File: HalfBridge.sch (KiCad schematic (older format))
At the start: 5 parts, among them Q2 Q_NMOS_DGS, Q3 Q_NMOS_DGS, Q4 STS8DN6LF6AG

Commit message: Started work on layout
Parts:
- removed Q2, Q3: Q_NMOS_DGS, symbol Device:Q_NMOS_DGS
- added D70, D71: LED_Green, LED_SMD:LED_0805_2012Metric_Pad1.15x1.40mm_HandSolder, symbol Custom-Symbols:LED_Green
- added Q20, Q21: DMN62D0U-7, Package_TO_SOT_SMD:SOT-23, symbol Custom-Symbols:DMN62D0U-7
- added R41, R42: R, Resistor_SMD:R_0805_2012Metric, symbol Device:R
- R3, R4: footprint (none) -> Resistor_SMD:R_0805_2012Metric
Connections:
- net labels added: +5V, Gate_H, Gate_L
- net labels removed: Power, VCC
- wire segments 23 -> 27
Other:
- note added: "Drive Status LEDs"
- note added: "Power MOSFET Datasheet:"
- moved on the sheet: Q22A, Q22B, R15, R16

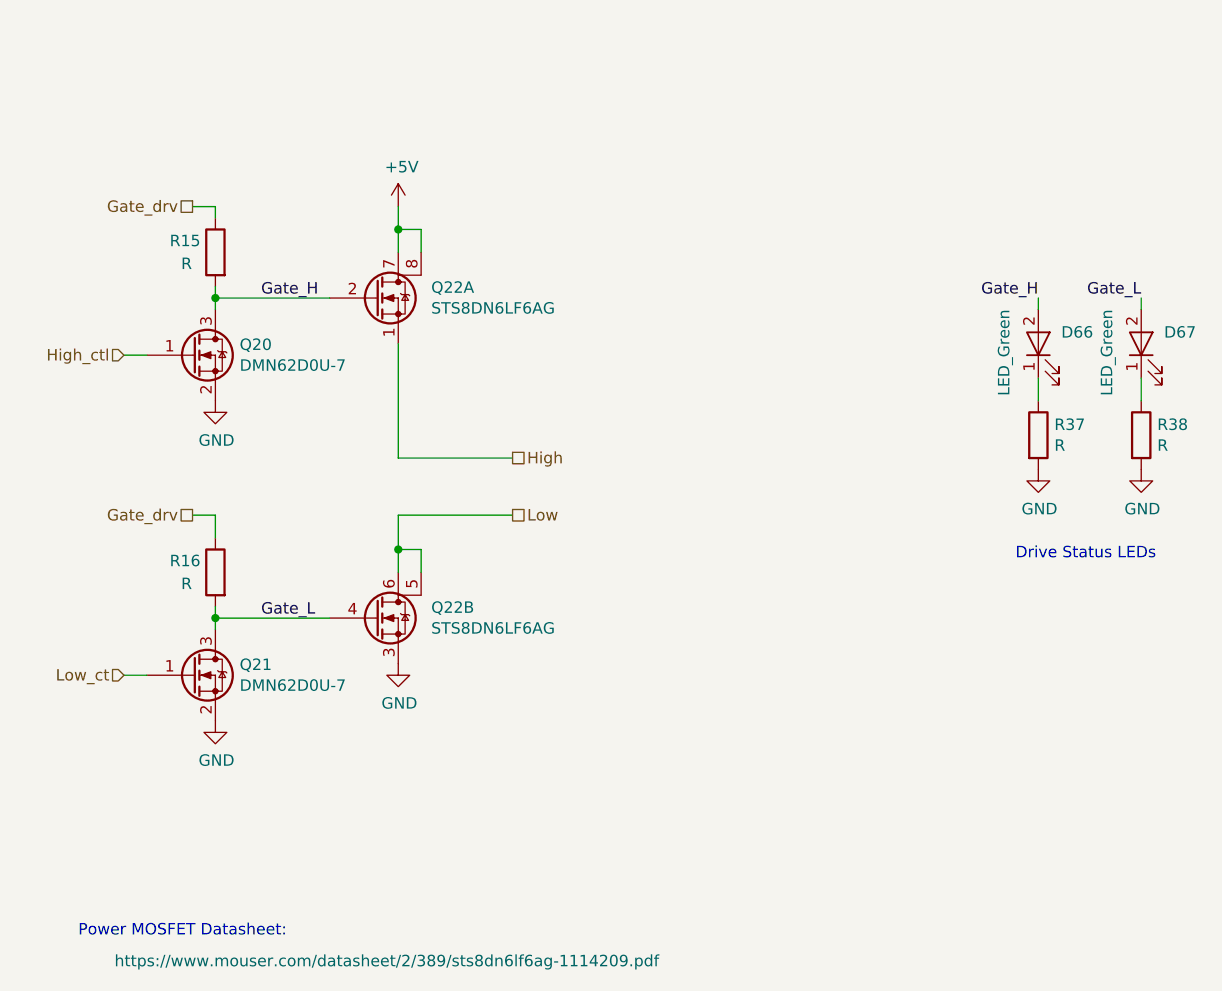
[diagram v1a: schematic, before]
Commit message: Fixed a footprint mistake
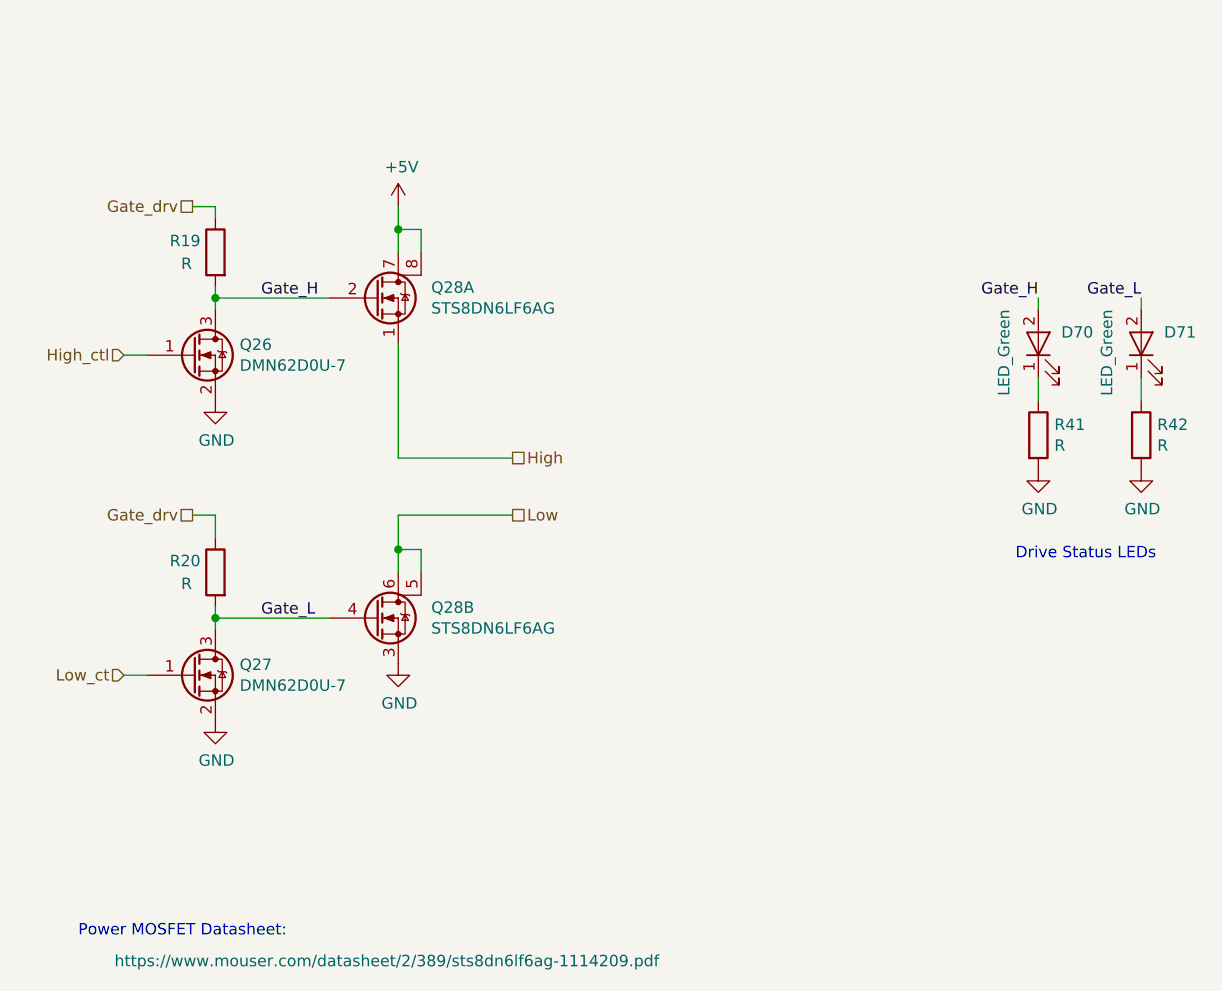
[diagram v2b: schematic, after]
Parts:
- Q4: footprint Package_SO:SO-8_5.3x6.2mm_P1.27mm -> Package_SO:SO-8_3.9x4.9mm_P1.27mm
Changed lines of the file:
@@
 EESchema Schematic File Version 4
-LIBS:flip-pixel-cache
-EELAYER 29 0
+EELAYER 30 0
 EELAYER END
 $Descr A 11000 8500
 encoding utf-8
-Sheet 9 12
+Sheet 11 12
 Title "Flip Pixel Board"
 Date "2020-06-20"
@@
 AR Path="/5EEA5FAB/5EE9876D" Ref="#PWR028"  Part="1"
 AR Path="/5EEA5FB2/5EE9876D" Ref="#PWR031"  Part="1"
-F 0 "#PWR022" H 3800 3200 50  0001 C CNN
+F 0 "#PWR031" H 3800 3200 50  0001 C CNN
 F 1 "GND" H 3805 3277 50  0000 C CNN
 F 2 "" H 3800 3450 50  0001 C CNN
@@
 AR Path="/5EEA5FAB/5EE98773" Ref="R19"  Part="1"
 AR Path="/5EEA5FB2/5EE98773" Ref="R21"  Part="1"
-F 0 "R15" H 4000 2850 50  0000 R CNN
+F 0 "R19" H 4000 2850 50  0000 R CNN
 F 1 "R" H 3950 2750 50  0000 R CNN
 F 2 "Resistor_SMD:R_0805_2012Metric" V 3730 2800 50  0001 C CNN
@@
 AR Path="/5EEA5FAB/5EE98786" Ref="#PWR029"  Part="1"
 AR Path="/5EEA5FB2/5EE98786" Ref="#PWR032"  Part="1"
-F 0 "#PWR023" H 3800 4600 50  0001 C CNN
+F 0 "#PWR032" H 3800 4600 50  0001 C CNN
 F 1 "GND" H 3805 4677 50  0000 C CNN
 F 2 "" H 3800 4850 50  0001 C CNN
@@
 AR Path="/5EEA5FAB/5EE9878C" Ref="R20"  Part="1"
 AR Path="/5EEA5FB2/5EE9878C" Ref="R22"  Part="1"
-F 0 "R16" H 4000 4250 50  0000 R CNN
+F 0 "R20" H 4000 4250 50  0000 R CNN
 F 1 "R" H 3950 4150 50  0000 R CNN
 F 2 "Resistor_SMD:R_0805_2012Metric" V 3730 4200 50  0001 C CNN
@@
 AR Path="/5EEA5FAB/5EE9879E" Ref="Q28"  Part="1"
 AR Path="/5EEA5FB2/5EE9879E" Ref="Q31"  Part="1"
-F 0 "Q22" H 4744 3046 50  0000 L CNN
+F 0 "Q28" H 4744 3046 50  0000 L CNN
 F 1 "STS8DN6LF6AG" H 4744 2955 50  0000 L CNN
-F 2 "Package_SO:SO-8_5.3x6.2mm_P1.27mm" H 4250 3500 50  0001 C CNN
+F 2 "Package_SO:SO-8_3.9x4.9mm_P1.27mm" H 4250 3500 50  0001 C CNN
 F 3 "https://www.mouser.com/datasheet/2/389/sts8dn6lf6ag-1114209.pdf" H 4550 100 50  0000 C CNN
 F 4 "497-17309-1-ND" H 3850 3350 50  0001 C CNN "Digikey-Part"
@@
 AR Path="/5EEA5FAB/5EE987A9" Ref="Q28"  Part="2"
 AR Path="/5EEA5FB2/5EE987A9" Ref="Q31"  Part="2"
-F 0 "Q22" H 4744 4446 50  0000 L CNN
+F 0 "Q28" H 4744 4446 50  0000 L CNN
 F 1 "STS8DN6LF6AG" H 4744 4355 50  0000 L CNN
-F 2 "Package_SO:SO-8_5.3x6.2mm_P1.27mm" H 4250 4900 50  0001 C CNN
+F 2 "Package_SO:SO-8_3.9x4.9mm_P1.27mm" H 4250 4900 50  0001 C CNN
 F 3 "https://www.mouser.com/datasheet/2/389/sts8dn6lf6ag-1114209.pdf" H 4700 4500 50  0001 C CNN
 F 4 "497-17309-1-ND" H 3850 4750 50  0001 C CNN "Digikey-Part"
@@
 AR Path="/5EEA5FAB/5EE987B3" Ref="#PWR030"  Part="1"
 AR Path="/5EEA5FB2/5EE987B3" Ref="#PWR033"  Part="1"
-F 0 "#PWR024" H 4600 4350 50  0001 C CNN
+F 0 "#PWR033" H 4600 4350 50  0001 C CNN
 F 1 "GND" H 4605 4427 50  0000 C CNN
 F 2 "" H 4600 4600 50  0001 C CNN
@@
 AR Path="/5EEA5FA4/5F3ABF0C" Ref="#PWR063"  Part="1"
 AR Path="/5EEA5FB2/5F3ABF0C" Ref="#PWR069"  Part="1"
-F 0 "#PWR060" H 4600 2450 50  0001 C CNN
+F 0 "#PWR069" H 4600 2450 50  0001 C CNN
 F 1 "+5V" H 4615 2773 50  0000 C CNN
 F 2 "" H 4600 2600 50  0001 C CNN
@@
 AR Path="/5EEA5FA4/5F3B0E6C" Ref="D68"  Part="1"
 AR Path="/5EEA5FB2/5F3B0E6C" Ref="D72"  Part="1"
-F 0 "D66" V 7450 3100 50  0000 R CNN
+F 0 "D70" V 7450 3100 50  0000 R CNN
 F 1 "LED_Green" H 7550 3350 50  0000 R CNN
 F 2 "LED_SMD:LED_0805_2012Metric_Pad1.15x1.40mm_HandSolder" H 7750 3650 50  0001 C CNN
@@
 AR Path="/5EEA5FA4/5F3B0E72" Ref="R39"  Part="1"
 AR Path="/5EEA5FB2/5F3B0E72" Ref="R43"  Part="1"
-F 0 "R37" H 7470 3646 50  0000 L CNN
+F 0 "R41" H 7470 3646 50  0000 L CNN
 F 1 "R" H 7470 3555 50  0000 L CNN
 F 2 "Resistor_SMD:R_0805_2012Metric" V 7330 3600 50  0001 C CNN
@@
 AR Path="/5EEA5FA4/5F3B0E78" Ref="#PWR064"  Part="1"
 AR Path="/5EEA5FB2/5F3B0E78" Ref="#PWR070"  Part="1"
-F 0 "#PWR061" H 7400 3500 50  0001 C CNN
+F 0 "#PWR070" H 7400 3500 50  0001 C CNN
 F 1 "GND" H 7405 3577 50  0000 C CNN
 F 2 "" H 7400 3750 50  0001 C CNN
@@
 AR Path="/5EEA5FA4/5F3B0E85" Ref="D69"  Part="1"
 AR Path="/5EEA5FB2/5F3B0E85" Ref="D73"  Part="1"
-F 0 "D67" V 7900 3100 50  0000 R CNN
+F 0 "D71" V 7900 3100 50  0000 R CNN
 F 1 "LED_Green" H 8000 3350 50  0000 R CNN
 F 2 "LED_SMD:LED_0805_2012Metric_Pad1.15x1.40mm_HandSolder" H 8200 3650 50  0001 C CNN
@@
 AR Path="/5EEA5FA4/5F3B0E8B" Ref="R40"  Part="1"
 AR Path="/5EEA5FB2/5F3B0E8B" Ref="R44"  Part="1"
-F 0 "R38" H 7920 3646 50  0000 L CNN
+F 0 "R42" H 7920 3646 50  0000 L CNN
 F 1 "R" H 7920 3555 50  0000 L CNN
 F 2 "Resistor_SMD:R_0805_2012Metric" V 7780 3600 50  0001 C CNN
@@
 AR Path="/5EEA5FA4/5F3B0E91" Ref="#PWR065"  Part="1"
 AR Path="/5EEA5FB2/5F3B0E91" Ref="#PWR071"  Part="1"
-F 0 "#PWR062" H 7850 3500 50  0001 C CNN
+F 0 "#PWR071" H 7850 3500 50  0001 C CNN
 F 1 "GND" H 7855 3577 50  0000 C CNN
 F 2 "" H 7850 3750 50  0001 C CNN
@@
 AR Path="/5EEA5FAB/5F506CAB" Ref="Q26"  Part="1"
 AR Path="/5EEA5FB2/5F506CAB" Ref="Q29"  Part="1"
-F 0 "Q20" H 3906 3296 50  0000 L CNN
+F 0 "Q26" H 3906 3296 50  0000 L CNN
 F 1 "DMN62D0U-7" H 3906 3205 50  0000 L CNN
 F 2 "Package_TO_SOT_SMD:SOT-23" H 3450 3950 50  0001 C CNN
@@
 AR Path="/5EEA5FAB/5F506FFC" Ref="Q27"  Part="1"
 AR Path="/5EEA5FB2/5F506FFC" Ref="Q30"  Part="1"
-F 0 "Q21" H 3906 4696 50  0000 L CNN
+F 0 "Q27" H 3906 4696 50  0000 L CNN
 F 1 "DMN62D0U-7" H 3906 4605 50  0000 L CNN
 F 2 "Package_TO_SOT_SMD:SOT-23" H 3450 5350 50  0001 C CNN

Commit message: Added 3D model to Power FET footprint
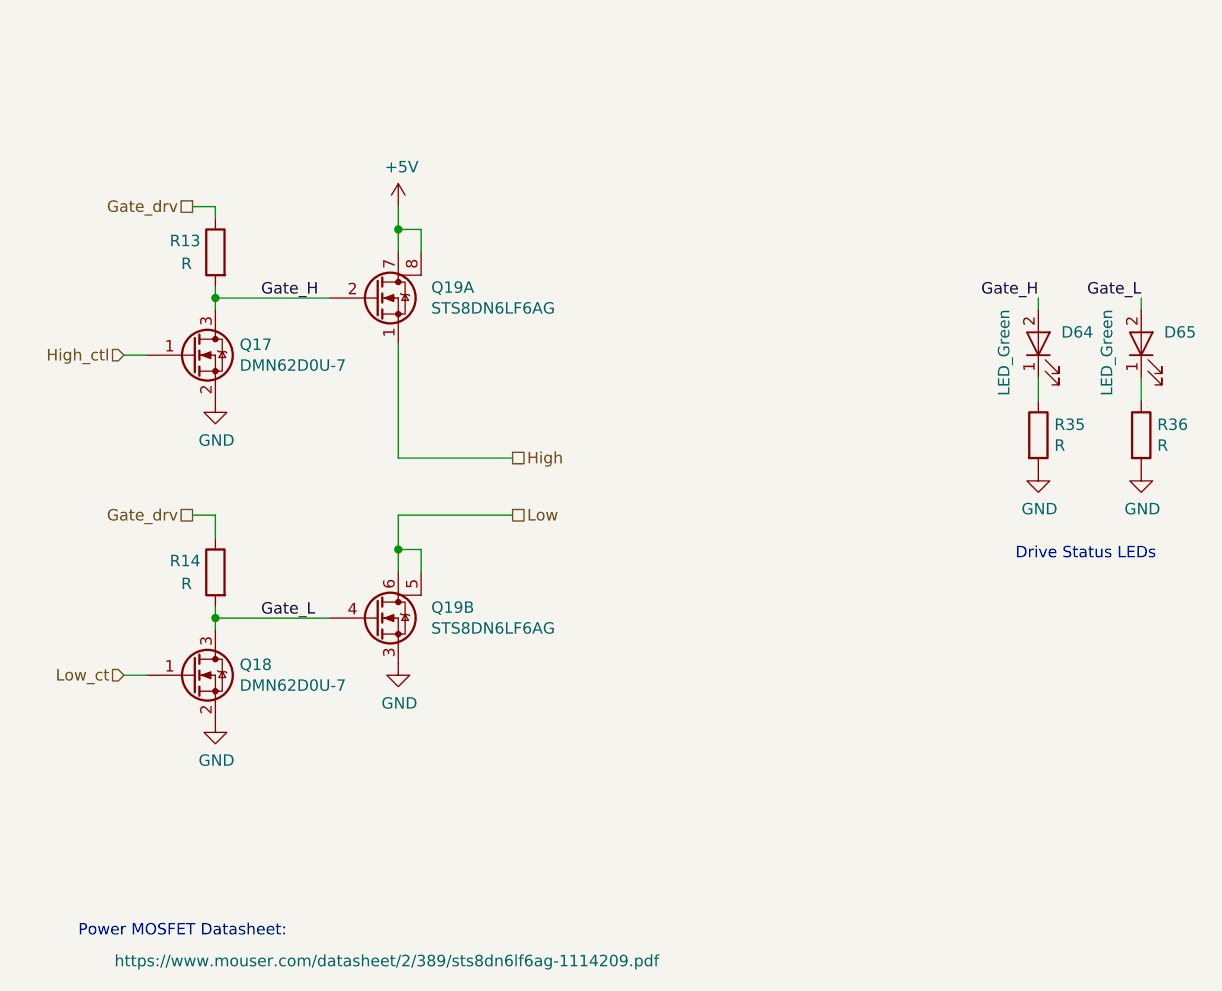
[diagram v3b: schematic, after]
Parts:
- Q4: footprint Package_SO:SO-8_3.9x4.9mm_P1.27mm -> Custom-Footprints:SO-8_3.9x4.9mm_P1.27mm
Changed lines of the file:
@@
 $Descr A 11000 8500
 encoding utf-8
-Sheet 11 12
+Sheet 8 12
 Title "Flip Pixel Board"
 Date "2020-06-20"
@@
 AR Path="/5EEA5FAB/5EE9876D" Ref="#PWR028"  Part="1"
 AR Path="/5EEA5FB2/5EE9876D" Ref="#PWR031"  Part="1"
-F 0 "#PWR031" H 3800 3200 50  0001 C CNN
+F 0 "#PWR019" H 3800 3200 50  0001 C CNN
 F 1 "GND" H 3805 3277 50  0000 C CNN
 F 2 "" H 3800 3450 50  0001 C CNN
@@
 AR Path="/5EEA5FAB/5EE98773" Ref="R19"  Part="1"
 AR Path="/5EEA5FB2/5EE98773" Ref="R21"  Part="1"
-F 0 "R19" H 4000 2850 50  0000 R CNN
+F 0 "R13" H 4000 2850 50  0000 R CNN
 F 1 "R" H 3950 2750 50  0000 R CNN
 F 2 "Resistor_SMD:R_0805_2012Metric" V 3730 2800 50  0001 C CNN
@@
 AR Path="/5EEA5FAB/5EE98786" Ref="#PWR029"  Part="1"
 AR Path="/5EEA5FB2/5EE98786" Ref="#PWR032"  Part="1"
-F 0 "#PWR032" H 3800 4600 50  0001 C CNN
+F 0 "#PWR020" H 3800 4600 50  0001 C CNN
 F 1 "GND" H 3805 4677 50  0000 C CNN
 F 2 "" H 3800 4850 50  0001 C CNN
@@
 AR Path="/5EEA5FAB/5EE9878C" Ref="R20"  Part="1"
 AR Path="/5EEA5FB2/5EE9878C" Ref="R22"  Part="1"
-F 0 "R20" H 4000 4250 50  0000 R CNN
+F 0 "R14" H 4000 4250 50  0000 R CNN
 F 1 "R" H 3950 4150 50  0000 R CNN
 F 2 "Resistor_SMD:R_0805_2012Metric" V 3730 4200 50  0001 C CNN
@@
 AR Path="/5EEA5FAB/5EE9879E" Ref="Q28"  Part="1"
 AR Path="/5EEA5FB2/5EE9879E" Ref="Q31"  Part="1"
-F 0 "Q28" H 4744 3046 50  0000 L CNN
+F 0 "Q19" H 4744 3046 50  0000 L CNN
 F 1 "STS8DN6LF6AG" H 4744 2955 50  0000 L CNN
-F 2 "Package_SO:SO-8_3.9x4.9mm_P1.27mm" H 4250 3500 50  0001 C CNN
+F 2 "Custom-Footprints:SO-8_3.9x4.9mm_P1.27mm" H 4250 3500 50  0001 C CNN
 F 3 "https://www.mouser.com/datasheet/2/389/sts8dn6lf6ag-1114209.pdf" H 4550 100 50  0000 C CNN
 F 4 "497-17309-1-ND" H 3850 3350 50  0001 C CNN "Digikey-Part"
@@
 AR Path="/5EEA5FAB/5EE987A9" Ref="Q28"  Part="2"
 AR Path="/5EEA5FB2/5EE987A9" Ref="Q31"  Part="2"
-F 0 "Q28" H 4744 4446 50  0000 L CNN
+F 0 "Q19" H 4744 4446 50  0000 L CNN
 F 1 "STS8DN6LF6AG" H 4744 4355 50  0000 L CNN
-F 2 "Package_SO:SO-8_3.9x4.9mm_P1.27mm" H 4250 4900 50  0001 C CNN
+F 2 "Custom-Footprints:SO-8_3.9x4.9mm_P1.27mm" H 4250 4900 50  0001 C CNN
 F 3 "https://www.mouser.com/datasheet/2/389/sts8dn6lf6ag-1114209.pdf" H 4700 4500 50  0001 C CNN
 F 4 "497-17309-1-ND" H 3850 4750 50  0001 C CNN "Digikey-Part"
@@
 AR Path="/5EEA5FAB/5EE987B3" Ref="#PWR030"  Part="1"
 AR Path="/5EEA5FB2/5EE987B3" Ref="#PWR033"  Part="1"
-F 0 "#PWR033" H 4600 4350 50  0001 C CNN
+F 0 "#PWR021" H 4600 4350 50  0001 C CNN
 F 1 "GND" H 4605 4427 50  0000 C CNN
 F 2 "" H 4600 4600 50  0001 C CNN
@@
 AR Path="/5EEA5FA4/5F3ABF0C" Ref="#PWR063"  Part="1"
 AR Path="/5EEA5FB2/5F3ABF0C" Ref="#PWR069"  Part="1"
-F 0 "#PWR069" H 4600 2450 50  0001 C CNN
+F 0 "#PWR057" H 4600 2450 50  0001 C CNN
 F 1 "+5V" H 4615 2773 50  0000 C CNN
 F 2 "" H 4600 2600 50  0001 C CNN
@@
 AR Path="/5EEA5FA4/5F3B0E6C" Ref="D68"  Part="1"
 AR Path="/5EEA5FB2/5F3B0E6C" Ref="D72"  Part="1"
-F 0 "D70" V 7450 3100 50  0000 R CNN
+F 0 "D64" V 7450 3100 50  0000 R CNN
 F 1 "LED_Green" H 7550 3350 50  0000 R CNN
 F 2 "LED_SMD:LED_0805_2012Metric_Pad1.15x1.40mm_HandSolder" H 7750 3650 50  0001 C CNN
@@
 AR Path="/5EEA5FA4/5F3B0E72" Ref="R39"  Part="1"
 AR Path="/5EEA5FB2/5F3B0E72" Ref="R43"  Part="1"
-F 0 "R41" H 7470 3646 50  0000 L CNN
+F 0 "R35" H 7470 3646 50  0000 L CNN
 F 1 "R" H 7470 3555 50  0000 L CNN
 F 2 "Resistor_SMD:R_0805_2012Metric" V 7330 3600 50  0001 C CNN
@@
 AR Path="/5EEA5FA4/5F3B0E78" Ref="#PWR064"  Part="1"
 AR Path="/5EEA5FB2/5F3B0E78" Ref="#PWR070"  Part="1"
-F 0 "#PWR070" H 7400 3500 50  0001 C CNN
+F 0 "#PWR058" H 7400 3500 50  0001 C CNN
 F 1 "GND" H 7405 3577 50  0000 C CNN
 F 2 "" H 7400 3750 50  0001 C CNN
@@
 AR Path="/5EEA5FA4/5F3B0E85" Ref="D69"  Part="1"
 AR Path="/5EEA5FB2/5F3B0E85" Ref="D73"  Part="1"
-F 0 "D71" V 7900 3100 50  0000 R CNN
+F 0 "D65" V 7900 3100 50  0000 R CNN
 F 1 "LED_Green" H 8000 3350 50  0000 R CNN
 F 2 "LED_SMD:LED_0805_2012Metric_Pad1.15x1.40mm_HandSolder" H 8200 3650 50  0001 C CNN
@@
 AR Path="/5EEA5FA4/5F3B0E8B" Ref="R40"  Part="1"
 AR Path="/5EEA5FB2/5F3B0E8B" Ref="R44"  Part="1"
-F 0 "R42" H 7920 3646 50  0000 L CNN
+F 0 "R36" H 7920 3646 50  0000 L CNN
 F 1 "R" H 7920 3555 50  0000 L CNN
 F 2 "Resistor_SMD:R_0805_2012Metric" V 7780 3600 50  0001 C CNN
@@
 AR Path="/5EEA5FA4/5F3B0E91" Ref="#PWR065"  Part="1"
 AR Path="/5EEA5FB2/5F3B0E91" Ref="#PWR071"  Part="1"
-F 0 "#PWR071" H 7850 3500 50  0001 C CNN
+F 0 "#PWR059" H 7850 3500 50  0001 C CNN
 F 1 "GND" H 7855 3577 50  0000 C CNN
 F 2 "" H 7850 3750 50  0001 C CNN
@@
 AR Path="/5EEA5FAB/5F506CAB" Ref="Q26"  Part="1"
 AR Path="/5EEA5FB2/5F506CAB" Ref="Q29"  Part="1"
-F 0 "Q26" H 3906 3296 50  0000 L CNN
+F 0 "Q17" H 3906 3296 50  0000 L CNN
 F 1 "DMN62D0U-7" H 3906 3205 50  0000 L CNN
 F 2 "Package_TO_SOT_SMD:SOT-23" H 3450 3950 50  0001 C CNN
@@
 AR Path="/5EEA5FAB/5F506FFC" Ref="Q27"  Part="1"
 AR Path="/5EEA5FB2/5F506FFC" Ref="Q30"  Part="1"
-F 0 "Q27" H 3906 4696 50  0000 L CNN
+F 0 "Q18" H 3906 4696 50  0000 L CNN
 F 1 "DMN62D0U-7" H 3906 4605 50  0000 L CNN
 F 2 "Package_TO_SOT_SMD:SOT-23" H 3450 5350 50  0001 C CNN
